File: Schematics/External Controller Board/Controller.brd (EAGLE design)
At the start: 101.3 x 81.3 mm, 11 parts, among them U1 TEENSY2, U2 JOYSTICK

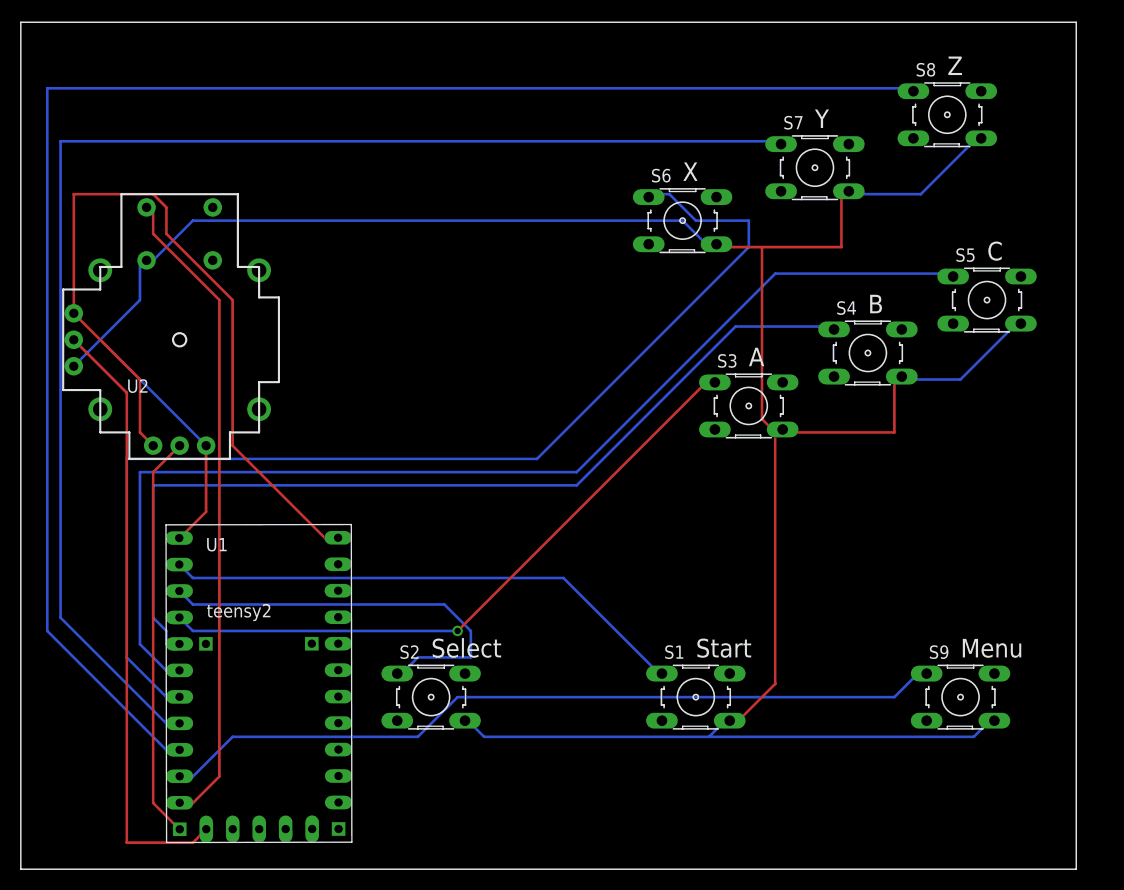
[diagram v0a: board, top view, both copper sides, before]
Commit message: External controller board updated.
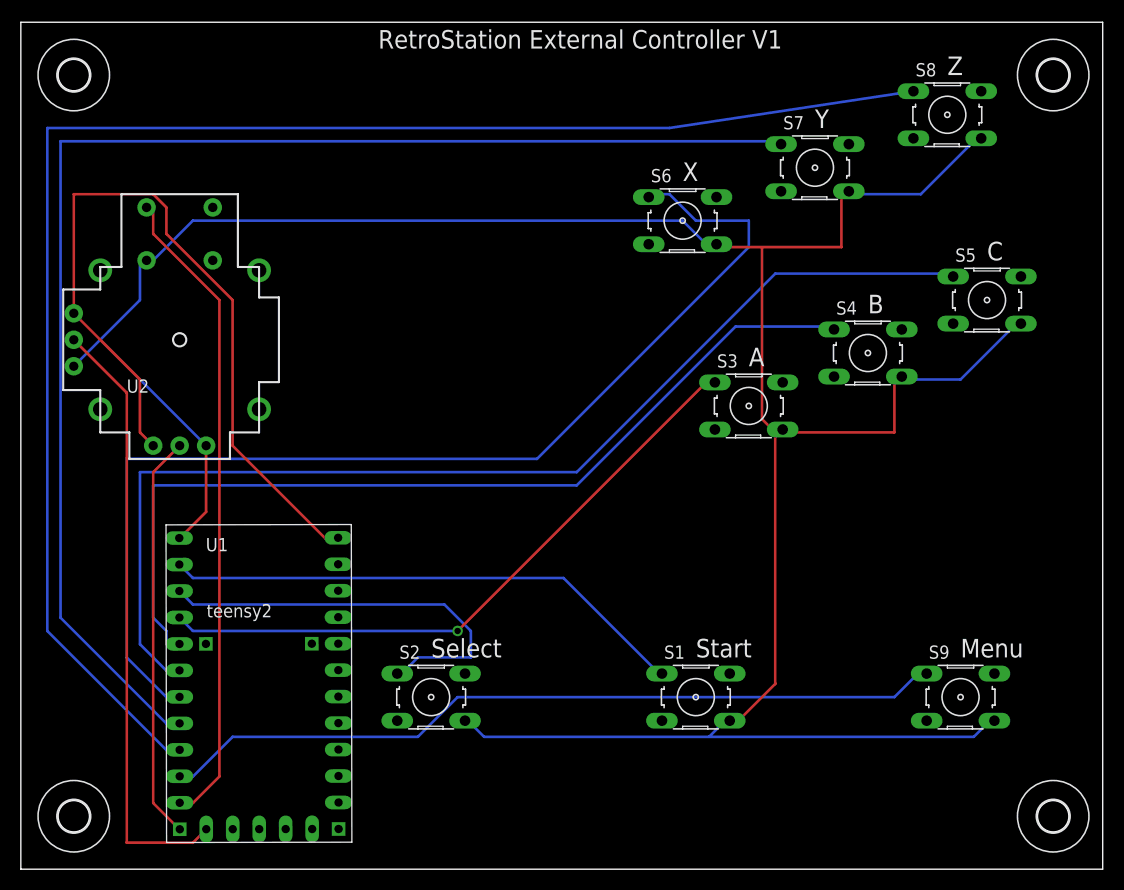
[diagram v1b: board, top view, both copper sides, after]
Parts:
- added U$1, U$2, U$3, U$4: (no value), holes:3,0
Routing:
- net N$8: track 152.7 -> 149.1 mm
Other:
- board size 101.3 x 81.3 mm -> 103.8 x 81.3 mm
- board text added: "RetroStation External Controller V1"
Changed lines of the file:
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@@
 <board>
 <plain>
-<wire x1="0" y1="0" x2="101.27" y2="0" width="0" layer="20"/>
-<wire x1="101.27" y1="0" x2="101.27" y2="81.27" width="0" layer="20"/>
-<wire x1="101.27" y1="81.27" x2="0" y2="81.27" width="0" layer="20"/>
+<wire x1="0" y1="0" x2="103.81" y2="0" width="0" layer="20"/>
+<wire x1="103.81" y1="0" x2="103.81" y2="81.27" width="0" layer="20"/>
+<wire x1="103.81" y1="81.27" x2="0" y2="81.27" width="0" layer="20"/>
 <wire x1="0" y1="81.27" x2="0" y2="0" width="0" layer="20"/>
 <text x="64.77" y="20.32" size="1.778" layer="25">Start</text>
@@
 <text x="88.9" y="76.2" size="1.778" layer="25">Z</text>
 <text x="90.17" y="20.32" size="1.778" layer="25">Menu</text>
+<text x="34.29" y="78.74" size="1.778" layer="25">RetroStation External Controller V1</text>
 </plain>
 <attributes>
@@
 <attribute name="OC_FARNELL" value="176432" x="90.17" y="16.51" size="1.778" layer="27" display="off"/>
 </element>
+<element name="U$1" library="holes" package="3,0" value="" x="99.06" y="5.08"/>
+<element name="U$2" library="holes" package="3,0" value="" x="5.08" y="5.08"/>
+<element name="U$3" library="holes" package="3,0" value="" x="99.06" y="76.2"/>
+<element name="U$4" library="holes" package="3,0" value="" x="5.08" y="76.2"/>
 </elements>
 <signals>
@@
 <contactref element="U1" pad="PD2"/>
 <wire x1="2.54" y1="22.86" x2="13.97" y2="11.43" width="0.254" layer="16"/>
-<wire x1="2.54" y1="74.93" x2="2.54" y2="22.86" width="0.254" layer="16"/>
-<wire x1="85.09" y1="74.93" x2="2.54" y2="74.93" width="0.254" layer="16"/>
+<wire x1="2.54" y1="71.12" x2="2.54" y2="22.86" width="0.254" layer="16"/>
+<wire x1="62.23" y1="71.12" x2="2.54" y2="71.12" width="0.254" layer="16"/>
 <wire x1="13.97" y1="11.43" x2="15.2377625" y2="11.4521625" width="0.254" layer="16"/>
-<wire x1="85.09" y1="74.93" x2="85.6488" y2="74.6506" width="0.254" layer="16"/>
+<wire x1="62.23" y1="71.12" x2="85.6488" y2="74.6506" width="0.254" layer="16"/>
 </signal>
 <signal name="N$9">

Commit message: Schematics updated External Controller board schematic created
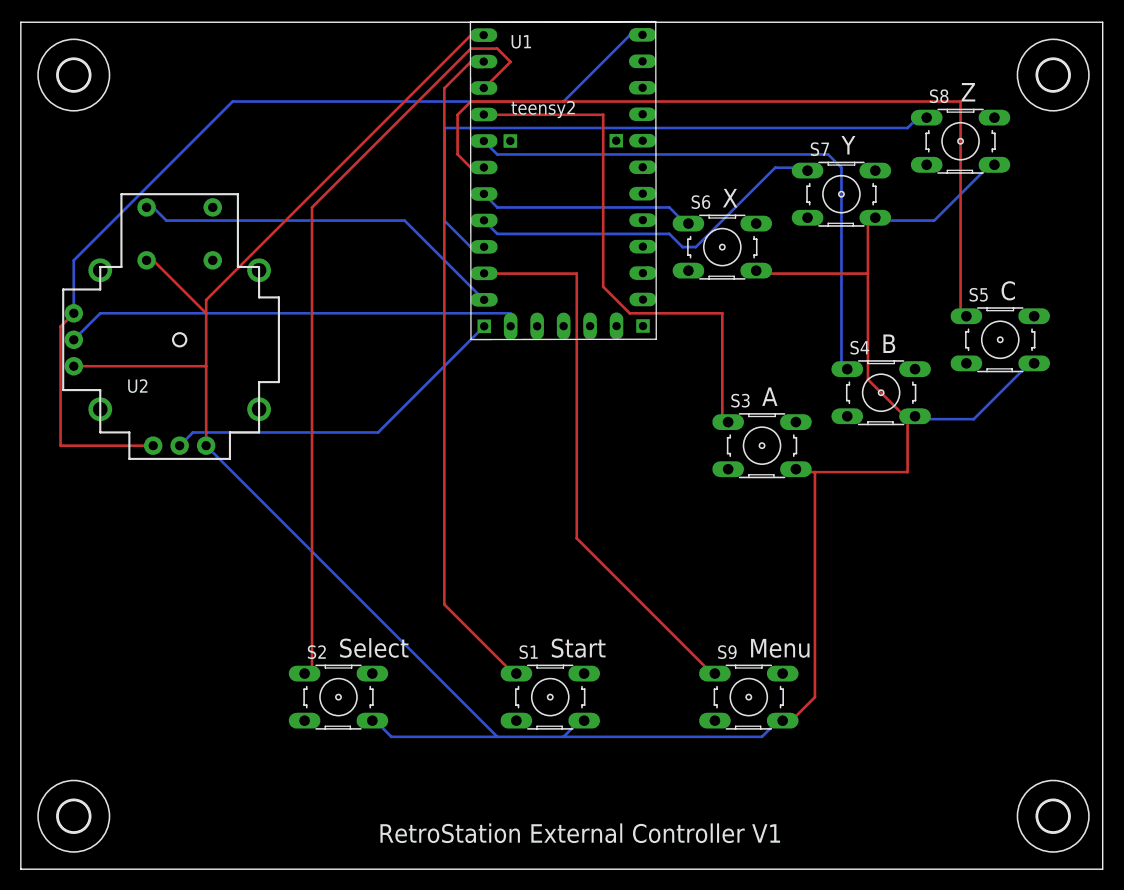
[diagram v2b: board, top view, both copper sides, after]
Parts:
- moved U1 56.4 mm to (31.8, 58.4)
- moved S9 20.3 mm to (69.8, 16.5)
- moved S1 14.0 mm to (50.8, 16.5)
- moved S2 8.89 mm to (30.5, 16.5)
- moved S6 4.58 mm to (67.3, 59.7)
- moved S3 4.02 mm to (71.1, 40.6)
- moved S5 4.02 mm to (94.0, 50.8)
- moved S4 4.02 mm to (82.5, 45.7)
- moved S7 3.59 mm to (78.7, 64.8)
- moved S8 2.84 mm to (90.2, 69.8)
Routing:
- net N$7: track 130.6 -> 35.3 mm
- net N$8: track 149.1 -> 60.6 mm
- net N$6: track 107.1 -> 20.8 mm
- net N$2: track 39.7 -> 74.7 mm
- net N$4: track 88.7 -> 55.0 mm
- net N$5: track 107.3 -> 76.6 mm
- net N$11: track 62.7 -> 36.1 mm
- net N$12: track 76.0 -> 52.9 mm
- net VCC: track 76.0 -> 90.7 mm
- net N$9: track 58.5 -> 44.2 mm
- net N$1: track 50.6 -> 64.0 mm
- net N$3: track 62.0 -> 51.2 mm, vias 1 -> 0
- net GND: track 262.0 -> 256.2 mm
- net N$10: track 39.0 -> 34.0 mm

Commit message: Updated the schematics for the external controller.
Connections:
- net GND renamed N$13
- net VCC renamed N$10
- removed net N$10 (its old number): U1.PC7, U2.H2
- removed net N$9 (its old number): U1.PD5, U2.V2
- new net N$11: U1.PF0, U2.H2
- new net N$14: U1.PF1, U2.V2
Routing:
- net N$11: track 0.00 -> 95.8 mm, vias 0 -> 1
- net N$14: track 0.00 -> 72.6 mm, vias 0 -> 1
- net N$13: track 256.2 -> 304.5 mm
- net N$9 (its old number): track 44.2 -> 0.00 mm
- net N$10 (its old number): track 34.0 -> 0.00 mm
- net N$10: track 90.7 -> 84.5 mm
